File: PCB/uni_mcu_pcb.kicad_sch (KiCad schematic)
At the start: 56 parts

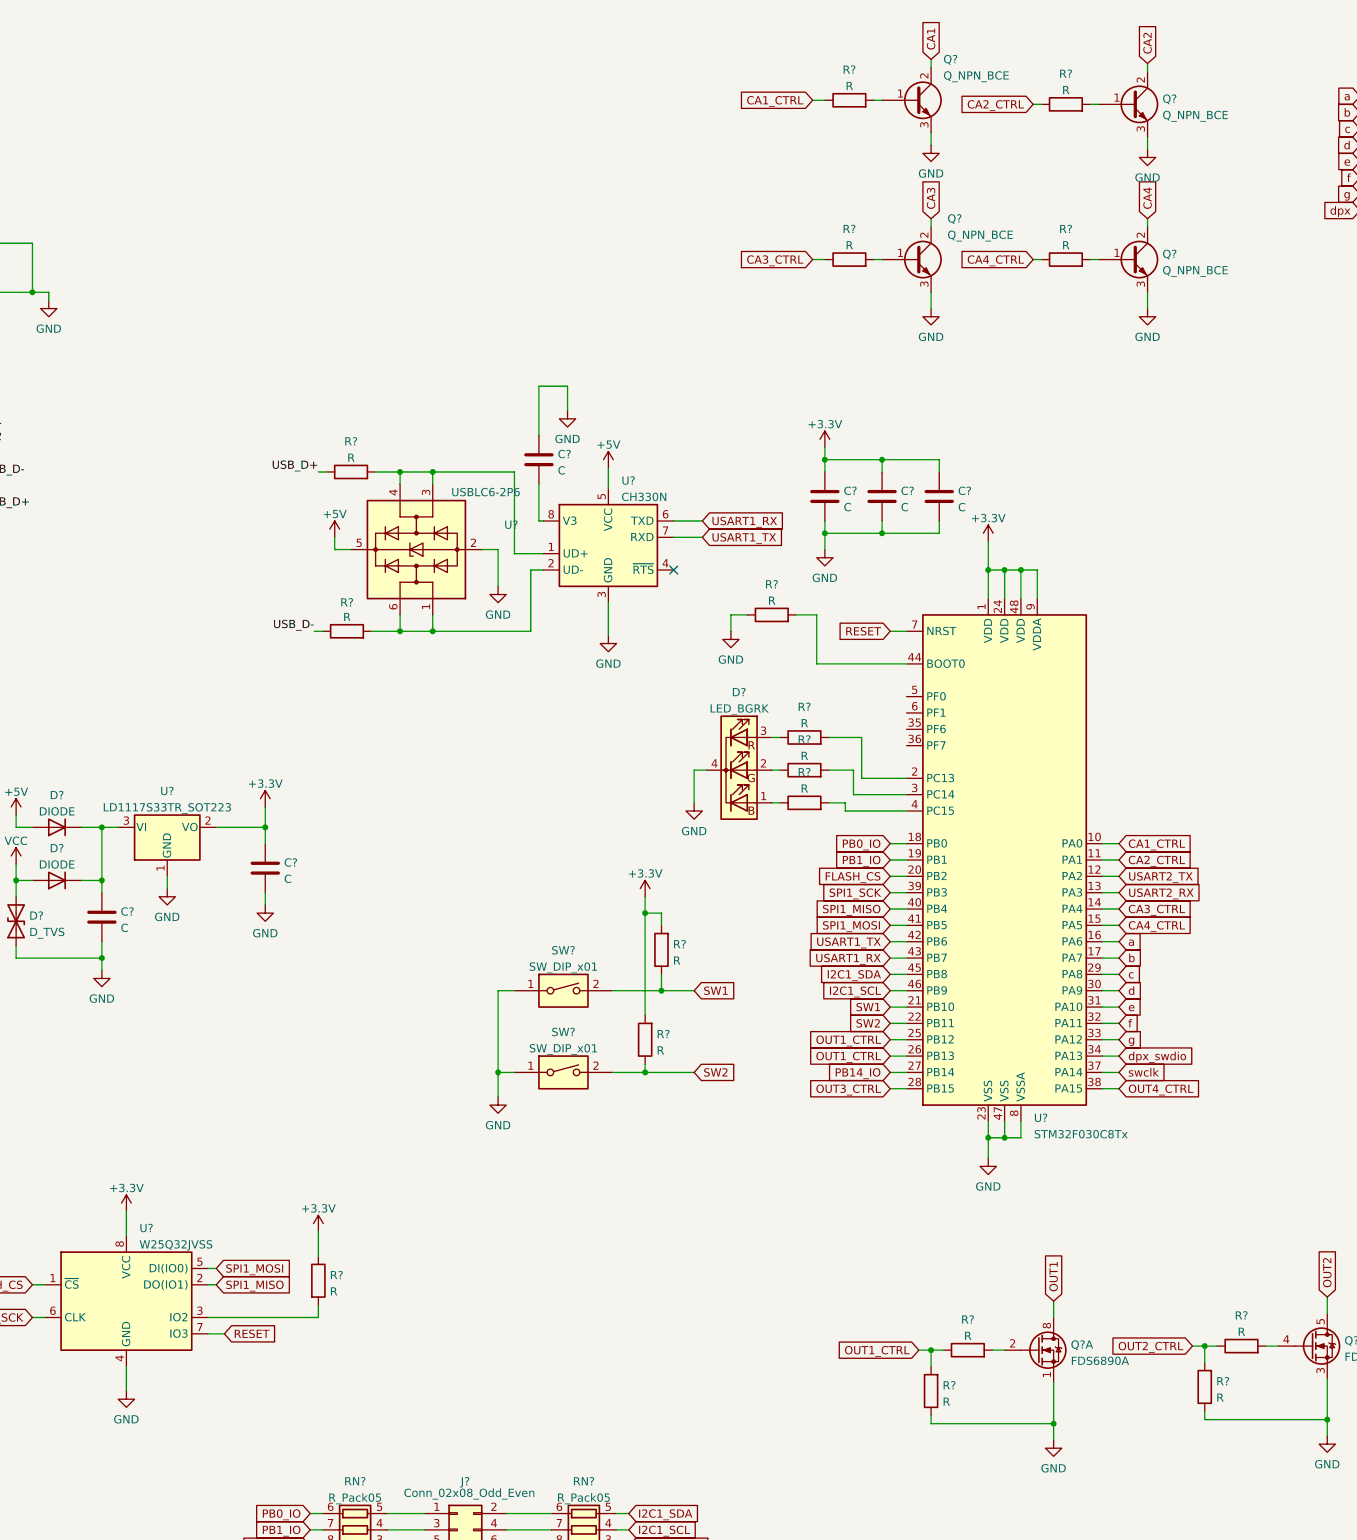
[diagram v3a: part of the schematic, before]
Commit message: Добавлен кварц. Нужно добавить модуль заряда
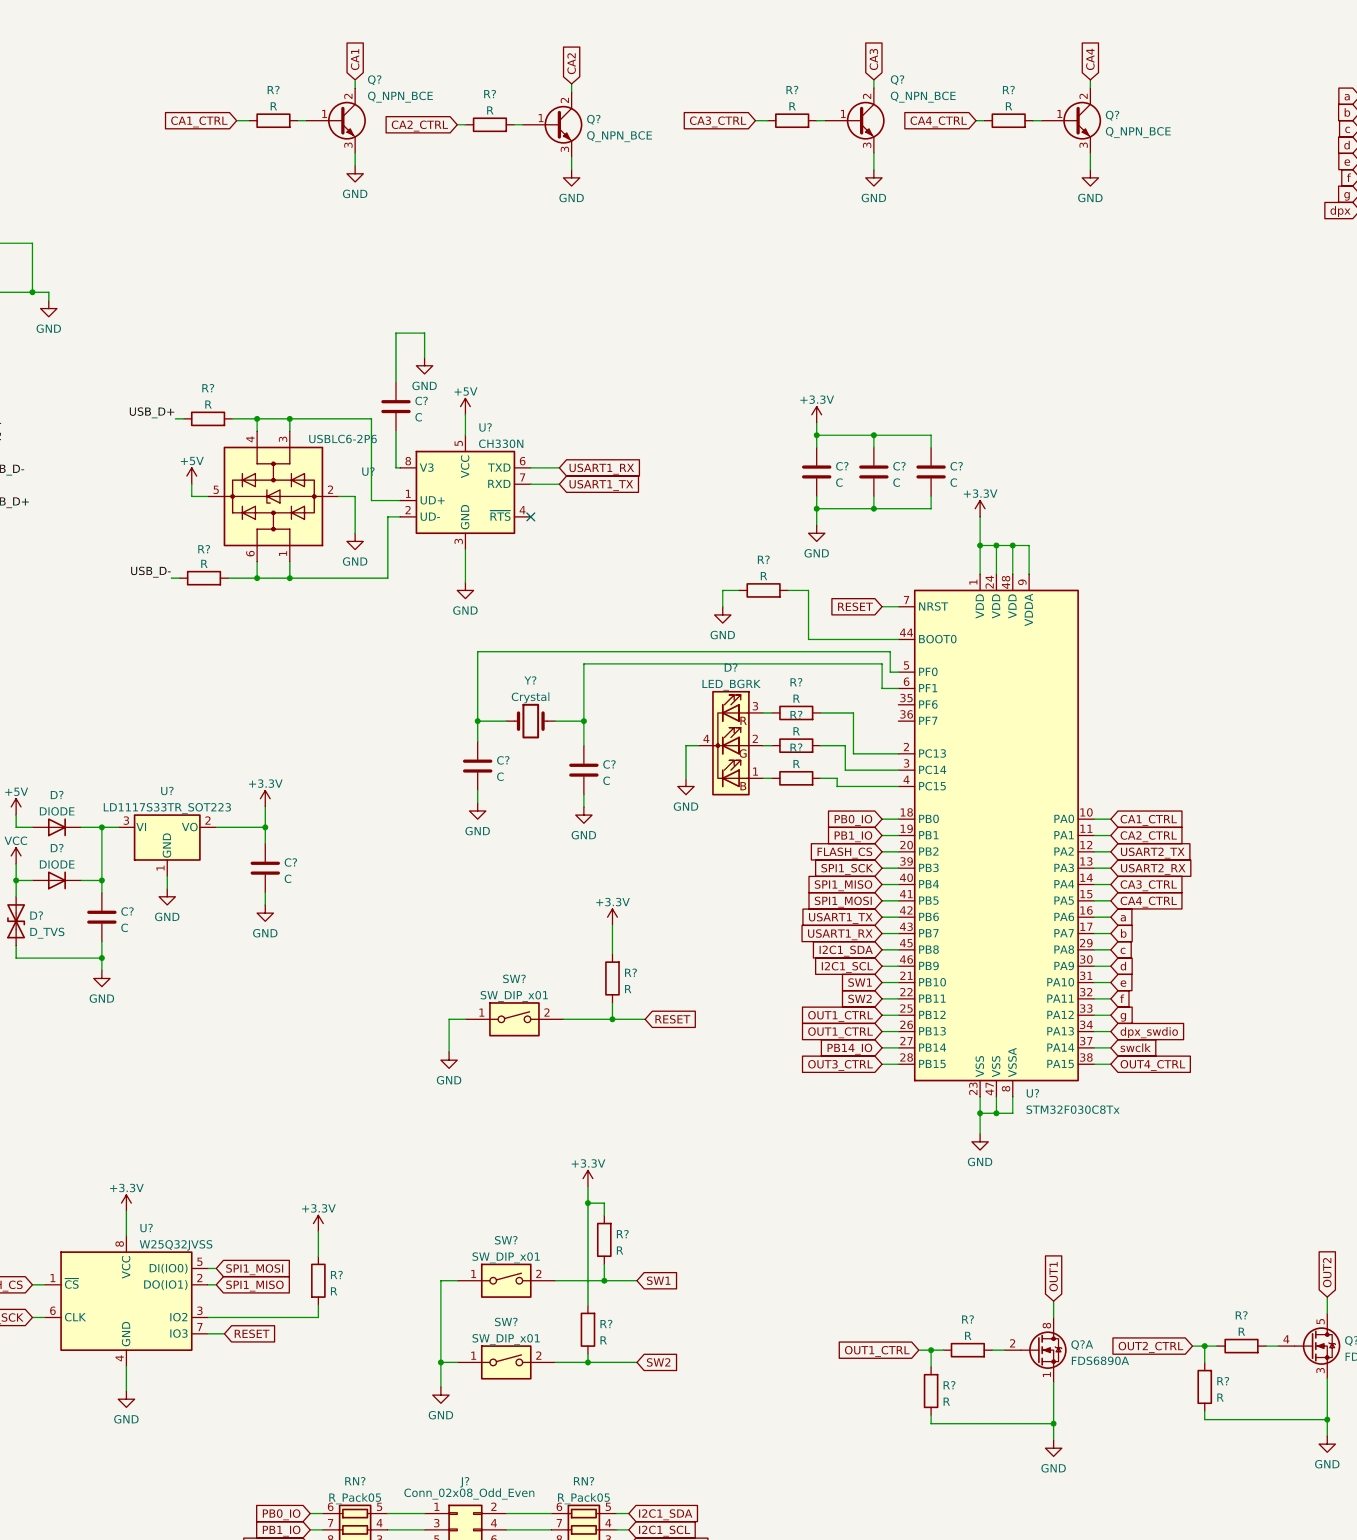
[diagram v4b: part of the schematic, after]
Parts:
- added C? (x2): C, symbol Device:C
- added R?: R, symbol Device:R
- added SW?: SW_DIP_x01, symbol Switch:SW_DIP_x01
- added Y?: Crystal, symbol Device:Crystal
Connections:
- net +3V3: now also R?.2
- net GND: now also C?.1, C?.2, SW?.1
- net RESET: now also R?.1, SW?.2
- net at U?.5 (PF0): now also C?.2, Y?.1
- net at U?.6 (PF1): now also C?.1, Y?.2
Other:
- moved on the sheet: C?, D?, Q?, R?, SW?, U?

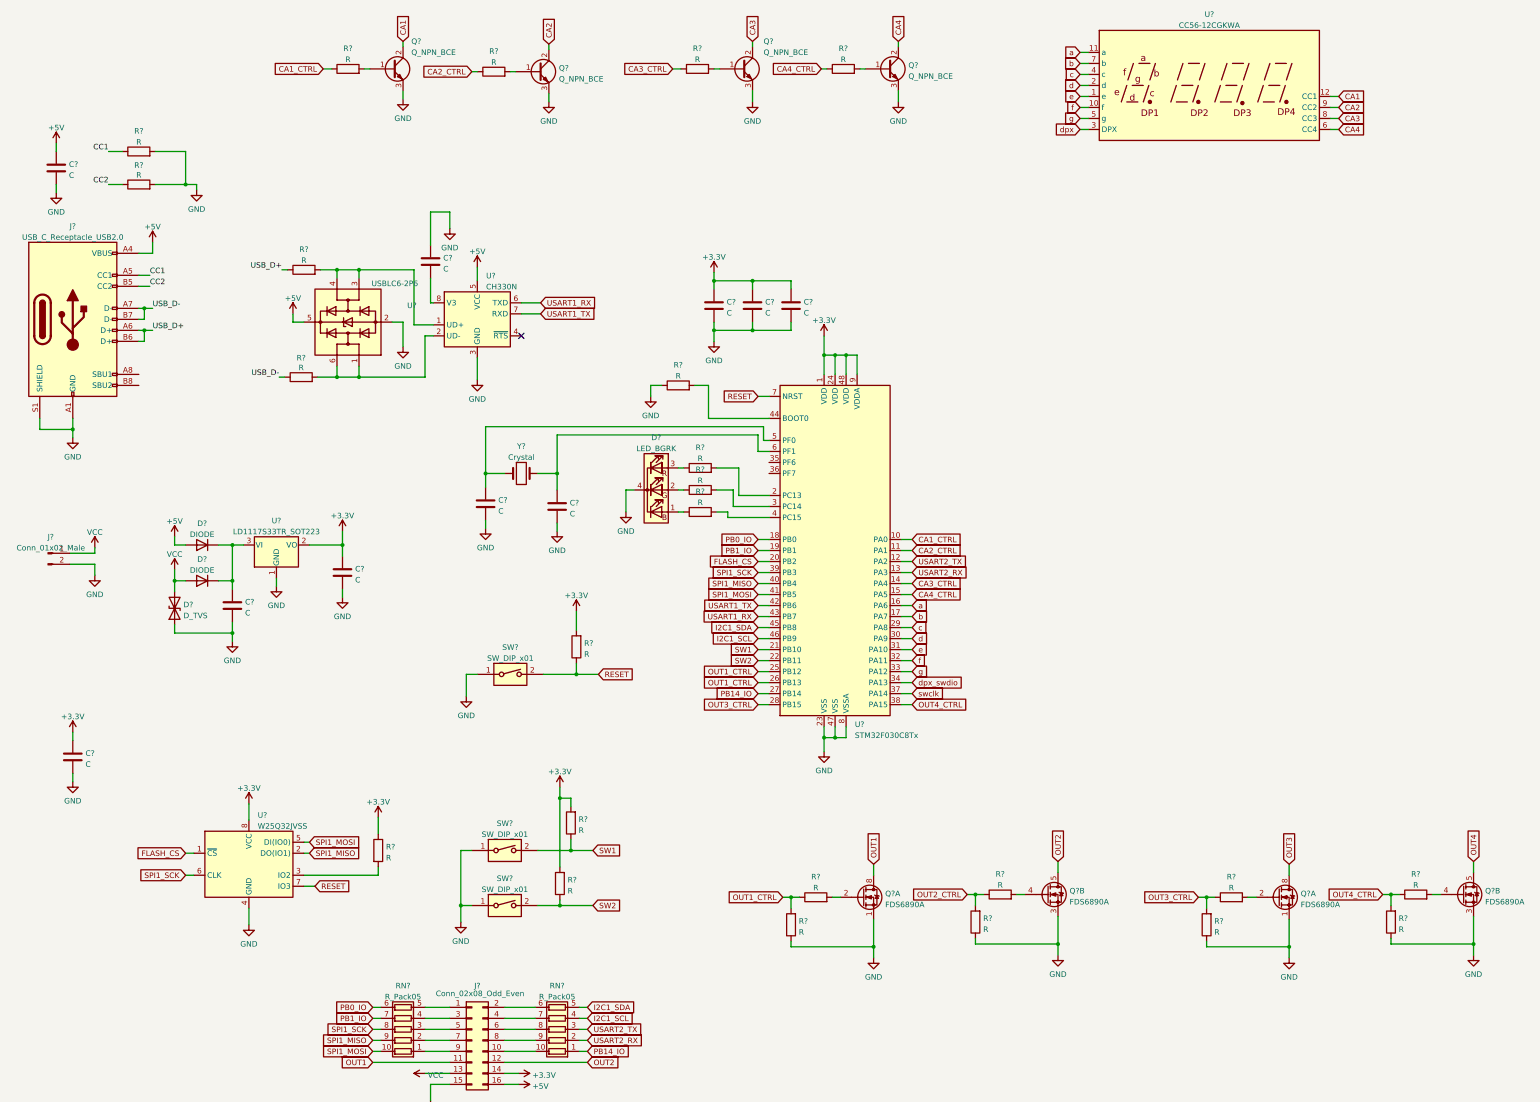
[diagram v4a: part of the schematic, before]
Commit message: Добавлен ещё один контроллер, но в QFP32 корпусе
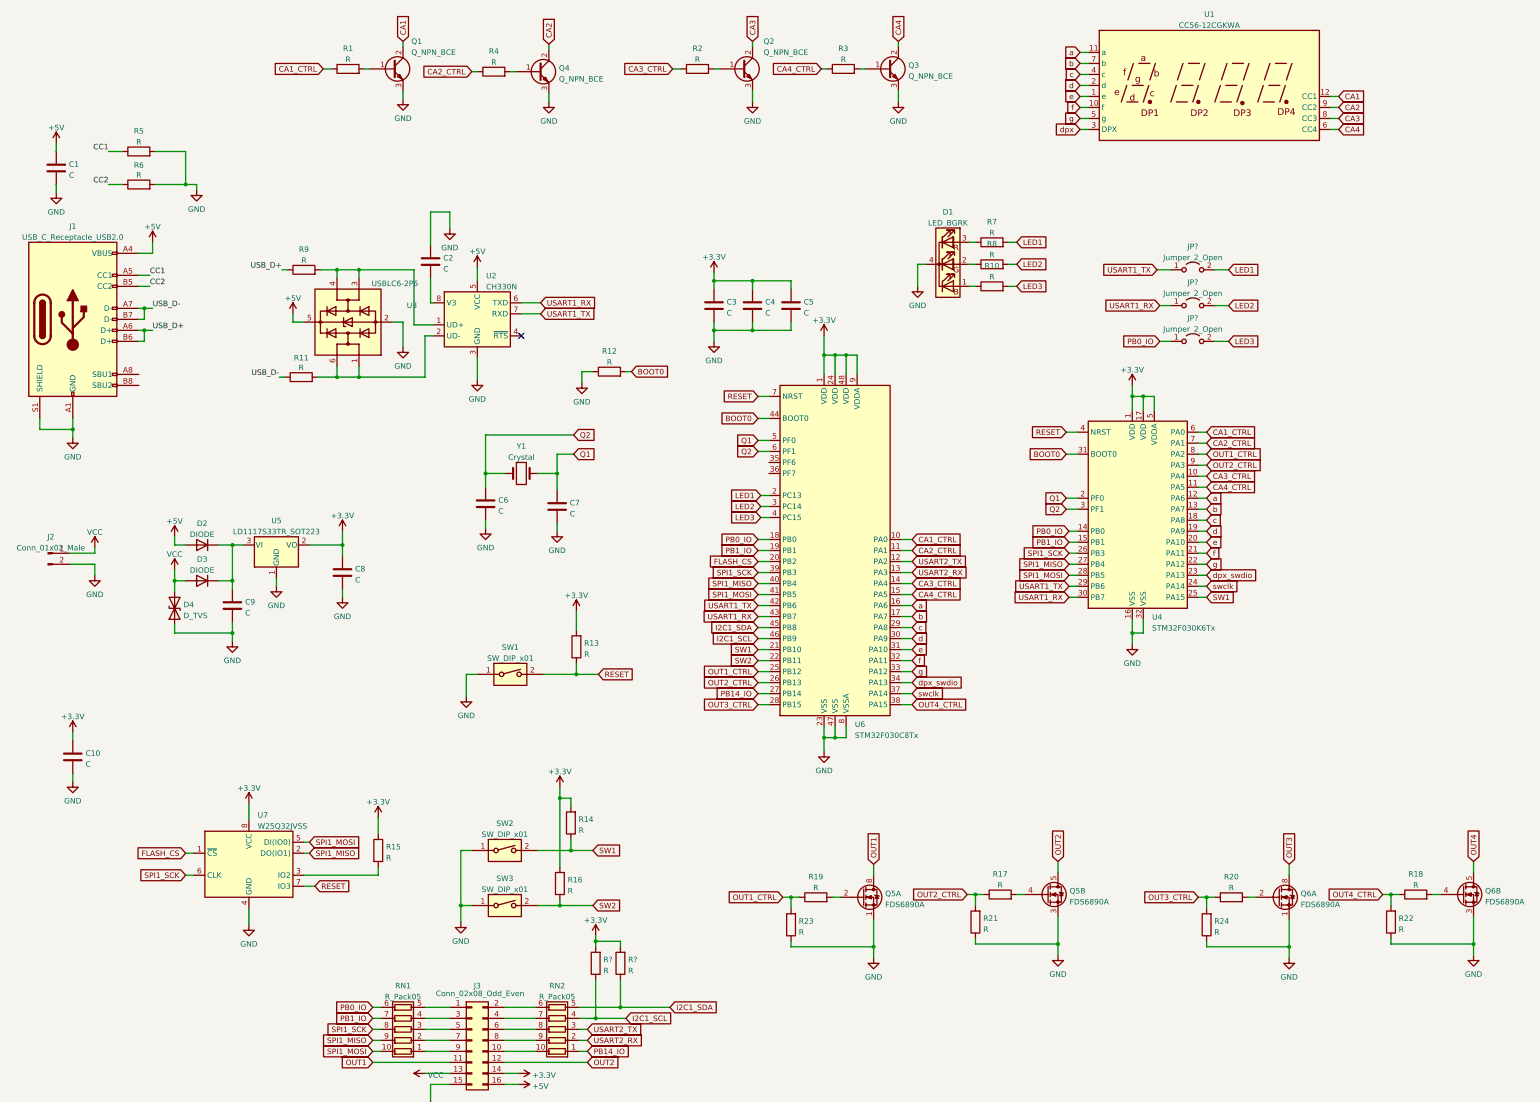
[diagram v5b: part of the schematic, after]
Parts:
- added JP? (x3): Jumper_2_Open, symbol Jumper:Jumper_2_Open
- added R? (x2): R, symbol Device:R
- added U4: STM32F030K6Tx, Package_QFP:LQFP-32_7x7mm_P0.8mm, symbol MCU_ST_STM32F0:STM32F030K6Tx
- gave numbers to parts that had none: 59
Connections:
- net +3V3: now also R?.2, R?.2, U4.1 (VDD), U4.17 (VDD), U4.5 (VDDA)
- net CA1_CTRL: now also U4.6 (PA0)
- net CA2_CTRL: now also U4.7 (PA1)
- net CA3_CTRL: now also U4.10 (PA4)
- net CA4_CTRL: now also U4.11 (PA5)
- net GND: now also U4.16 (VSS), U4.32 (VSS)
- net I2C1_SCL: now also R?.1
- net I2C1_SDA: now also R?.1
- net OUT1_CTRL: now also U4.8 (PA2); no longer U6.26 (PB13)
- net OUT2_CTRL: now also U6.26 (PB13), U4.9 (PA3)
- net PB0_IO: now also JP?.1 (A), U4.14 (PB0)
- net PB1_IO: now also U4.15 (PB1)
- net RESET: now also U4.4 (NRST)
- net SPI1_MISO: now also U4.27 (PB4)
- net SPI1_MOSI: now also U4.28 (PB5)
- net SPI1_SCK: now also U4.26 (PB3)
- net SW1: now also U4.25 (PA15)
- net USART1_RX: now also JP?.1 (A), U4.30 (PB7)
- net USART1_TX: now also JP?.1 (A), U4.29 (PB6)
- net a: now also U4.12 (PA6)
- net b: now also U4.13 (PA7)
- net c: now also U4.18 (PA8)
- net d: now also U4.19 (PA9)
- net dpx_swdio: now also U4.23 (PA13)
- net e: now also U4.20 (PA10)
- net f: now also U4.21 (PA11)
- net g: now also U4.22 (PA12)
- net swclk: now also U4.24 (PA14)
- net LED1: now reaches R7.2, U6.2 (PC13)
- net LED1: now also JP?.2 (B)
- net LED2: now reaches R8.2, U6.3 (PC14)
- net LED2: now also JP?.2 (B)
- net BOOT0: now reaches R12.2, U6.44 (BOOT0)
- net BOOT0: now also U4.31 (BOOT0)
- net Q2: now reaches C6.2, Y1.1
- net Q2: now also U6.6 (PF1), U4.3 (PF1); no longer U6.5 (PF0)
- net Q1: now reaches C7.1, Y1.2
- net Q1: now also U6.5 (PF0), U4.2 (PF0); no longer U6.6 (PF1)
- net LED3: now reaches R10.2, U6.4 (PC15)
- net LED3: now also JP?.2 (B)
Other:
- moved on the sheet: D1, R10, R12, R7, R8

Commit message: Начата разводка платы
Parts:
- C1, C10, C2, C3, C4, C5, C6, C7, C8, C9: footprint (none) -> Capacitor_SMD:C_0603_1608Metric_Pad1.08x0.95mm_HandSolder
- D1: footprint (none) -> LED_SMD:LED_RGB_1210
- D2, D3, D4: footprint (none) -> Diode_SMD:D_SMB
- J1: footprint (none) -> Connector_USB:USB_C_Receptacle_GCT_USB4105-xx-A_16P_TopMnt_Horizontal
- J2: footprint (none) -> Connector_PinHeader_2.54mm:PinHeader_1x02_P2.54mm_Vertical
- J3: footprint (none) -> Connector_IDC:IDC-Header_2x08_P2.54mm_Vertical
- JP1, JP2, JP3: renamed from JP?; footprint (none) -> Jumper:SolderJumper-2_P1.3mm_Open_TrianglePad1.0x1.5mm
- Q1, Q2, Q3, Q4: footprint (none) -> Package_TO_SOT_SMD:SOT-23-3
- R1, R10, R11, R12, R13, R14, R15, R16, R17, R18, R19, R2, R20, R21, R22, R23, R24, R3, R4, R5, R6, R7, R8, R9: footprint (none) -> Resistor_SMD:R_0603_1608Metric_Pad0.98x0.95mm_HandSolder
- R25, R26: renamed from R?; footprint (none) -> Resistor_SMD:R_0603_1608Metric_Pad0.98x0.95mm_HandSolder
- RN1, RN2: footprint (none) -> Resistor_SMD:R_Array_Convex_5x0603
- SW1, SW2, SW3: footprint (none) -> Button_Switch_SMD:SW_Push_1P1T_NO_Vertical_Wuerth_434133025816
- Y1: footprint (none) -> Crystal:Crystal_HC49-4H_Vertical

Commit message: Добавлены библиотеки для зарядки li-ion
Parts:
- added U?: DW01, symbol mcuDebugBoard:DW01
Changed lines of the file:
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@@
     (pin "3")
+  )
+  (symbol (lib_id "mcuDebugBoard:DW01") (at 354.965 127.635 0) (unit 1)
+    (in_bom yes) (on_board yes) (fields_autoplaced)
+    (property "Reference" "U?" (id 0) (at 355.6 117.2009 0)
+      (effects (font (size 1.524 1.524)))
+    )
+    (property "Value" "DW01" (id 1) (at 355.6 120.1943 0)
+      (effects (font (size 1.524 1.524)))
+    )
+    (property "Footprint" "" (id 2) (at 353.695 135.255 0)
+      (effects (font (size 1.524 1.524)) hide)
+    )
+    (property "Datasheet" "" (id 3) (at 353.695 135.255 0)
+      (effects (font (size 1.524 1.524)) hide)
+    )
+    (pin "1")
+    (pin "2")
+    (pin "3")
+    (pin "4")
+    (pin "5")
+    (pin "6")
   )
   (symbol (lib_id "power:+3.3V") (at 280.67 111.125 0) (unit 1)
@@
       (reference "U7") (unit 1) (value "W25Q32JVSS") (footprint "Package_SO:SOIC-8_5.23x5.23mm_P1.27mm")
     )
+    (path "/a9e687d5-0bce-4b5f-ba69-7f9457e5fd72"
+      (reference "U?") (unit 1) (value "DW01") (footprint "")
+    )
     (path "/94a95235-74c5-4cbc-9998-dd9ada7362c9"
